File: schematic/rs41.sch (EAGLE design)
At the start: 267 parts, among them J201 SENSORBOOM, Q201 BSS92, Q202 BSS92, Q203 BSS101, Q204 BSS101, Q501 BSS92, Q502 BSS101, Q503 BSS101, Q601 BSS101, U101 STM32F100C8T6B, U201 TS3A4751, U202 TS5A9411, U203 TS5A9411, U204 TS5A9411, U205 74HCU04, U206 305G, U207 74LVC3G34, U208 Z27F, U301 DIFFGEN, U302 UBX-6010MLF56, U303 SAW, U304 LNA, U401 SI4032QFN204X4, U501 TLV70030SOT23-5, U502 TPS61200, U503 TLV70030SOT23-5, U504 TLV70030SOT23-5, U601 25AA080SN, X101 24MHz, X301 OSC_GPSXTAL4

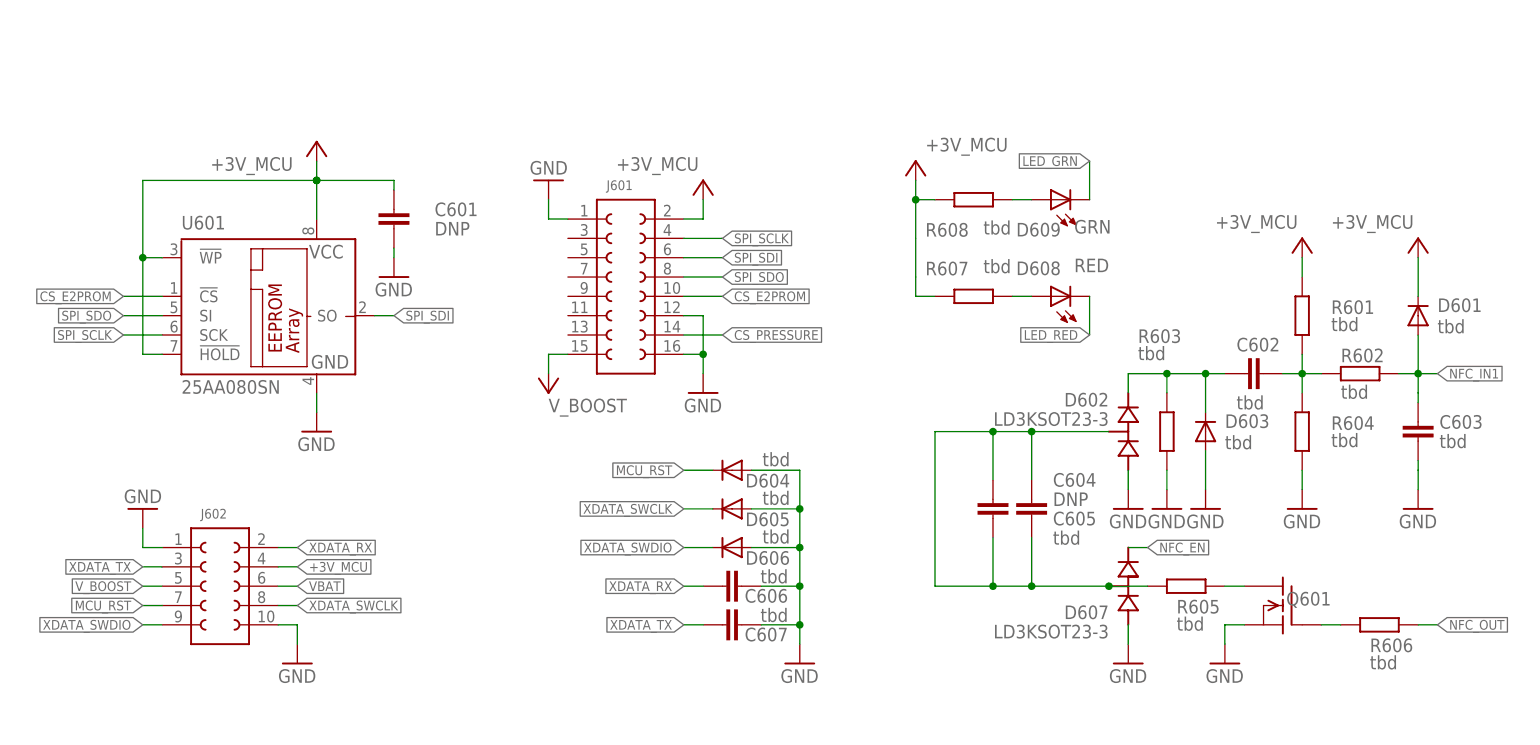
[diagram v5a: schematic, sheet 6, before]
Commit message: rearanged interface sheet
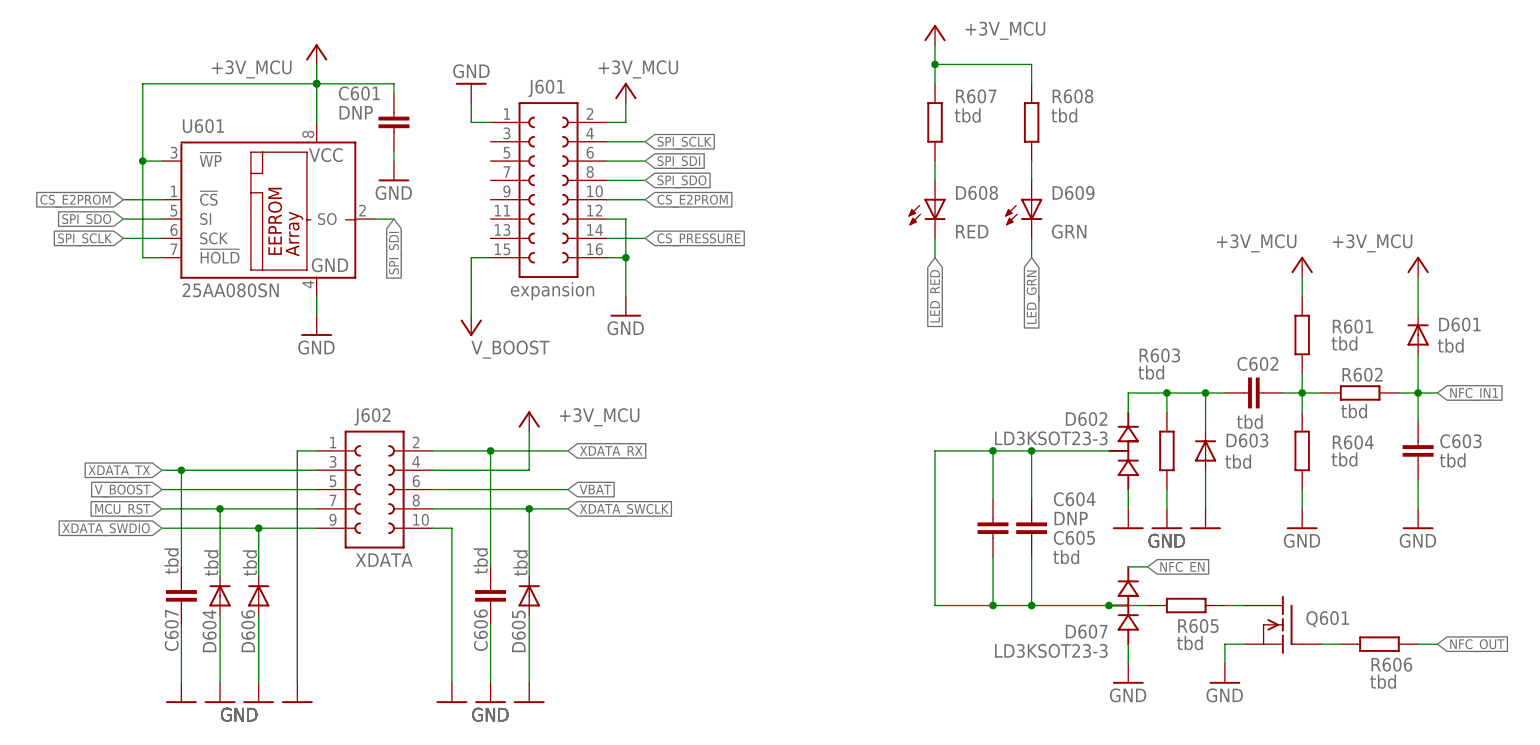
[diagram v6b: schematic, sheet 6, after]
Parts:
- J601: value (none) -> expansion
- J602: value (none) -> XDATA
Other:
- moved on the sheet: C601, C602, C603, C604, C605, C606, C607, D601, D602, D603, D604, D605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

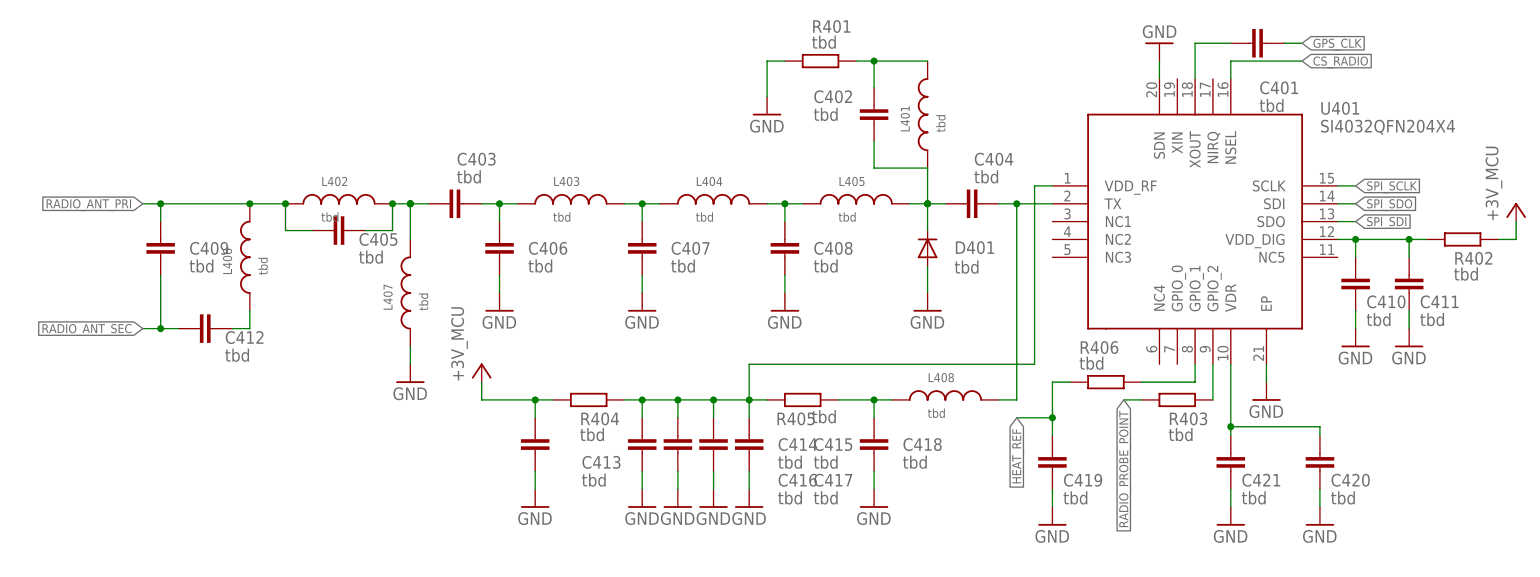
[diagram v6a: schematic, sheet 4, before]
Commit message: added resistor values and corrected GPS Pin 12
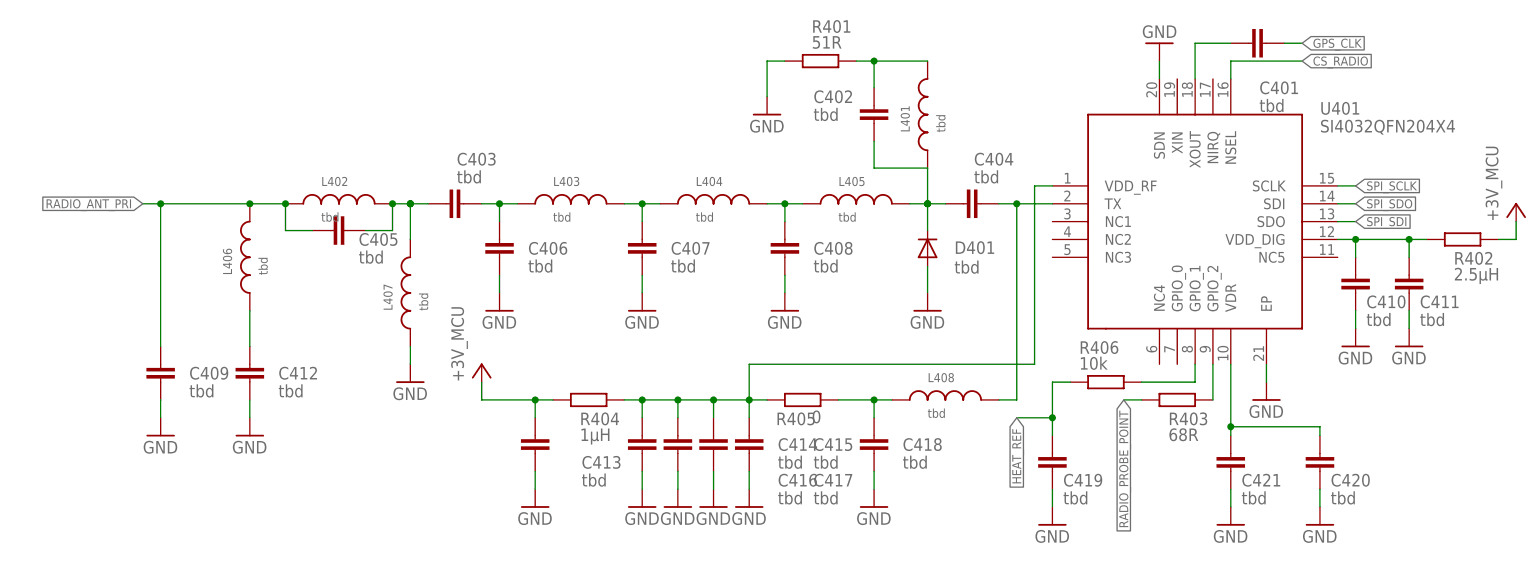
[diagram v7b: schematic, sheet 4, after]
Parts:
- R101, R117, R507, R602: value tbd -> 1k
- R102, R112, R115, R119, R120, R121, R122, R224, R225, R309, R403: value tbd -> 68R
- R103, R104, R106, R118, R125, R213, R219, R220, R406, R501, R506, R603: value tbd -> 10k
- R105, R107, R108, R109, R114, R126, R303, R508, R509, R512, R513: value tbd -> 47k
- R110, R116, R305, R306, R307, R608: value tbd -> 100R
- R111: value tbd -> 1.9µH
- R113: value tbd -> 2.1µH
- R123, R223, R226, R308: value tbd -> 3.9k
- R201, R202, R203: value (none) -> 100R; device rcl:R-EU_R0402 -> rcl:R-EU_R0603
- R204, R205: value (none) -> 150R; device rcl:R-EU_R0402 -> rcl:R-EU_R0603
- R207: value tbd -> 1,01k; device rcl:R-EU_R0402 -> rcl:R-EU_R0805
- R208: value tbd -> 750R; device rcl:R-EU_R0402 -> rcl:R-EU_R0805
- R209: value tbd -> 10k termistor
- R210: value tbd -> 39R
- R211: value tbd -> 62R
- R212: value tbd -> 34.8k
- R214: value tbd -> 330R
- R215: value tbd -> 237R
- R216, R217, R218: value tbd -> 30R; device rcl:R-EU_R0402 -> rcl:R-EU_R0603
- R221, R222: value tbd -> 1R
- R301, R302: value tbd -> 2.7µH
- R304, R405: value tbd -> 0
- R401, R607: value tbd -> 51R
- R402: value tbd -> 2.5µH
- R404: value tbd -> 1µH
- R503, R604: value tbd -> 330k
- R504: value tbd -> 51k
- R505: value tbd -> 20k
- R510: value tbd -> 178k
- R511, R601: value tbd -> 100k
- R514: value tbd -> 62k
- R605: value tbd -> 240R
- R606: value tbd -> 10R
- renumbered R502 to F502
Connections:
- removed net RADIO_ANT_SEC: C409.1, C412.2
- net GND: now also C409.1, C412.2, U302.VDD_USB
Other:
- moved on the sheet: C314, C409, C412

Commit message: started adding c values
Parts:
- C101: value tbd -> 10u; device rcl:C-EUC0402 -> rcl:C-EUC0603
- C102, C103, C104, C106, C108, C111, C112, C214: value tbd -> 100n
- C105, C115, C117, C118, C119, C120, C121, C122, C123: value tbd -> 12p
- C107: value tbd -> 1u
- C109, C110: value tbd -> 15n
- C113, C114, C124, C208, C210, C211, C220, C221: value tbd -> 27p
- C116, C201, C202, C203, C204, C205, C206, C217: value tbd -> 10n
- C207, C215: value tbd -> 1n
- C209: value tbd -> 47p; device rcl:C-EUC0402 -> rcl:C-EUC0603
- C212: value tbd -> 8.2n; device rcl:C-EUC0402 -> rcl:C-EUC0603
- C213: value tbd -> 330p
- C216: value tbd -> 270p
